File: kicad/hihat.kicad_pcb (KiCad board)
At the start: 2 copper layers, 174.5 x 173.5 mm, 172 parts, among them J1 Synth_power_2x5, J10 brain_south, J11 CVin, J2 CH trig, J3 accent, J4 CH out, J5 ctrl_north, J6 brain_north, J7 OH trig, J8 OH out, J9 ctrl_south, Q1 BC556, Q10 BC546, Q11 BC546, Q12 BC546, Q13 BC546, Q14 2N3904, Q15 BC546, Q16 BC546, Q2 BC546, Q3 BC546, Q4 BC556, Q5 BC556, Q6 BC556, Q7 BC546, Q8 BC546, Q9 BC546, SW1 mute, U1 TL074, U2 LM7805_TO220, U4 TL074, U5 LM13700, U6 Vactrol, U7 40106, U8 TL074

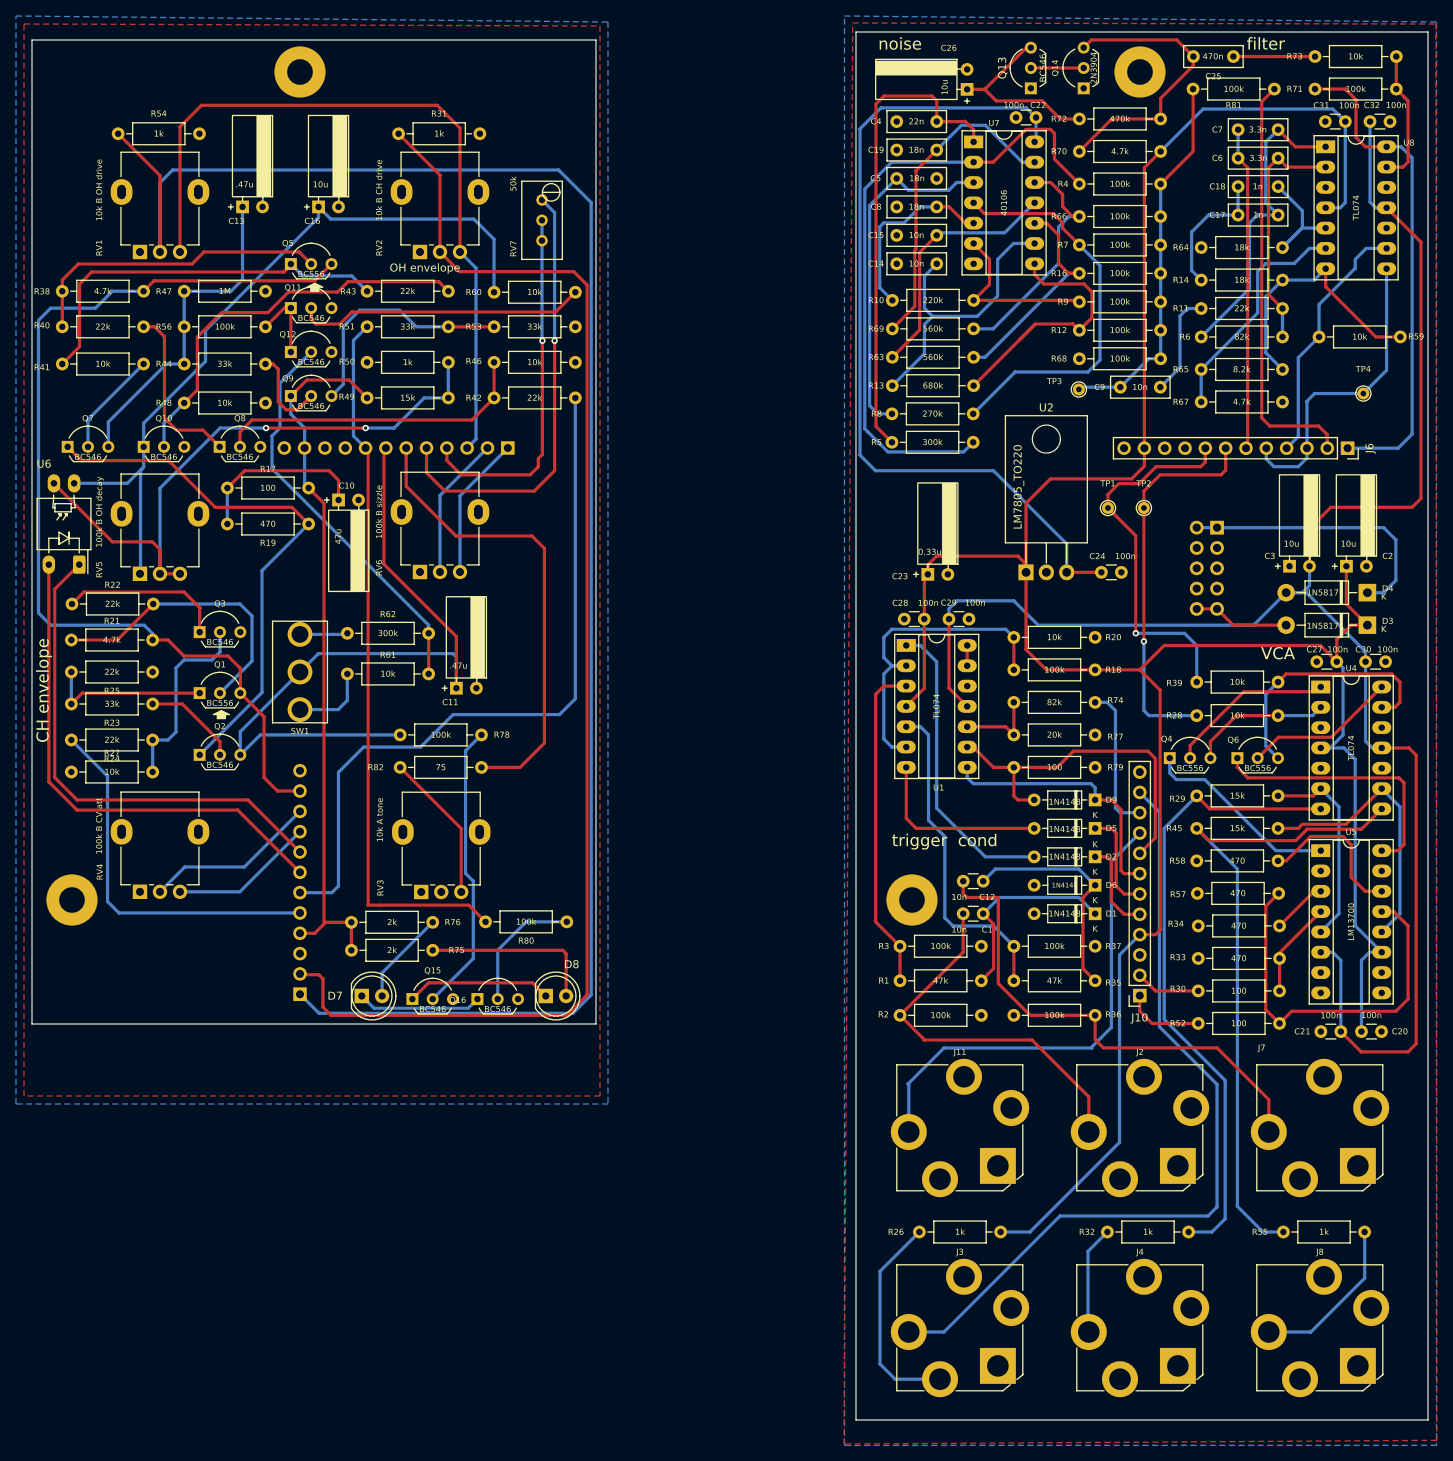
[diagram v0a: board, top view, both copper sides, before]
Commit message: fix noise section (1uF instead of 10uF), location of switch jacks!!, add resistor to make sizzle pot log-like and add note to use socket for cap to adjust tight decay
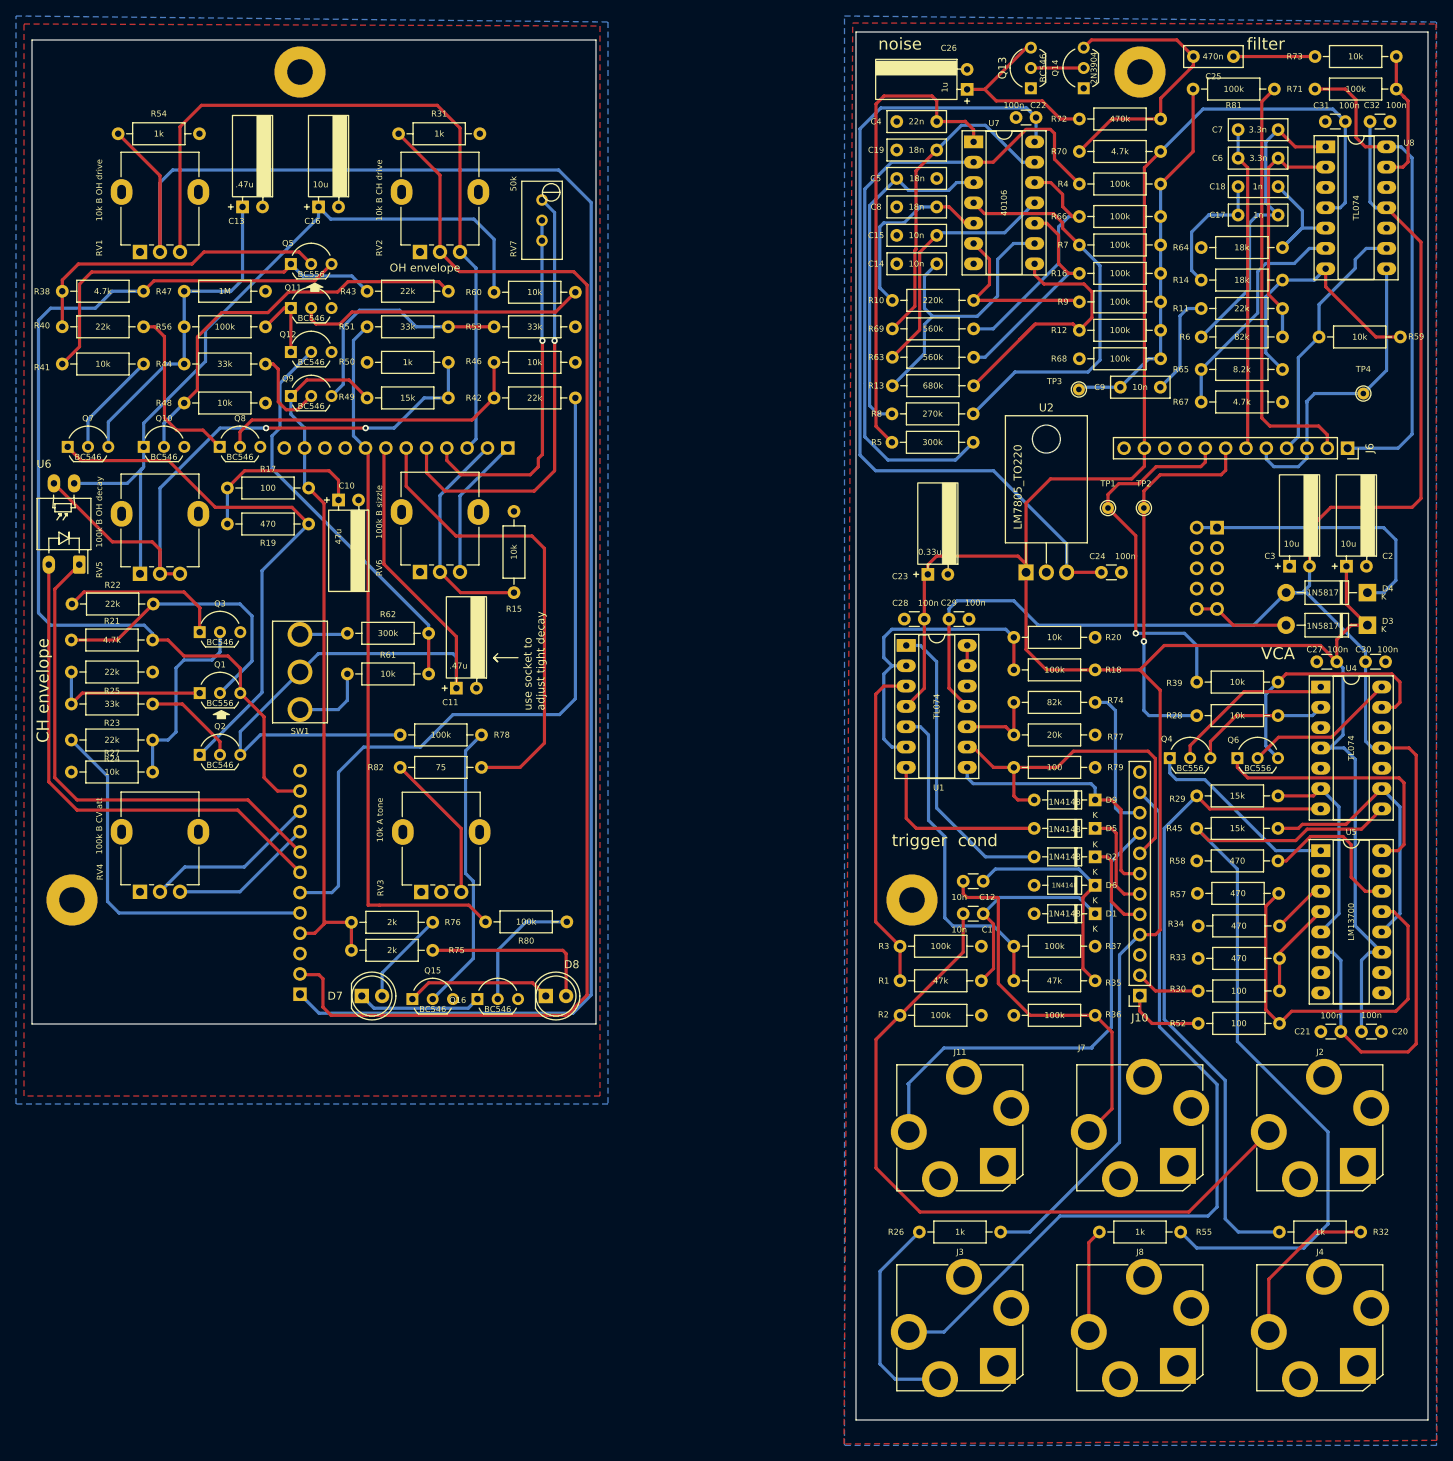
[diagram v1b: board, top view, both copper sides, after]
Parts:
- added R15: 10k, ao_tht:R_Axial_DIN0207_L6.3mm_D2.5mm_P10.16mm_Horizontal, F.Cu at (79.2, 100.6)
- C26: value 10u -> 1u
- moved R55 33.2 mm to (152.4, 180.5), turned to 0 degrees
- moved R32 31.7 mm to (185.1, 180.5), turned to 180 degrees
- moved J2 22.5 mm to (180.0, 167.5)
- moved J4 22.5 mm to (180.0, 192.5)
- moved J7 22.5 mm to (157.5, 167.5)
- moved J8 22.5 mm to (157.5, 192.5)
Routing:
- net Net-(C1-Pad2): track 48.2 -> 91.8 mm
- net Net-(R45-Pad1): track 81.8 -> 102.1 mm
- net Net-(C12-Pad2): track 62.5 -> 47.3 mm
- net white_noise_att_ctrl: track 18.0 -> 28.3 mm
- net Net-(J8-PadT): track 20.6 -> 13.0 mm
- net Net-(J4-PadT): track 13.5 -> 20.5 mm
- net Net-(R29-Pad1): track 79.1 -> 81.3 mm
- net Net-(R4-Pad1): track 79.7 -> 81.1 mm
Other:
- board text added: "use socket to adjust tight decay"

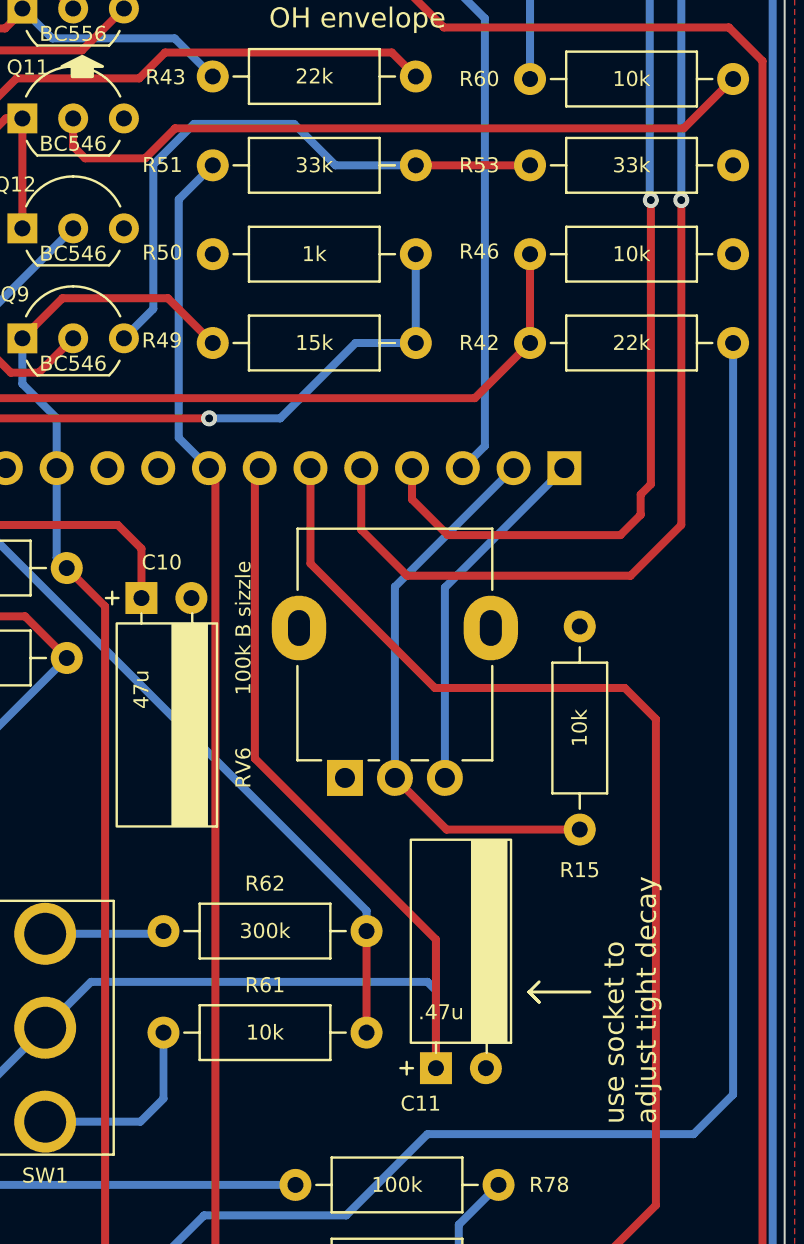
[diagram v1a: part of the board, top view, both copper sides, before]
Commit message: remove R51, now the open hat is much louder!
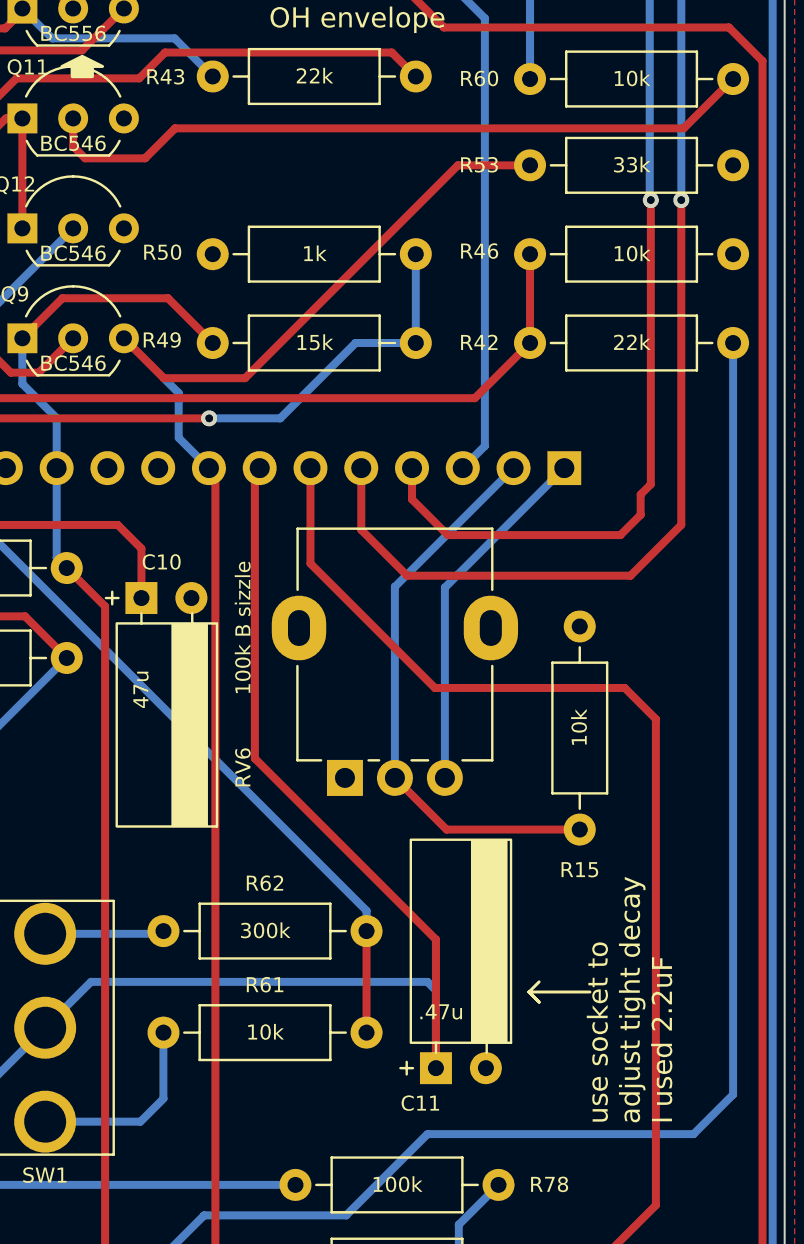
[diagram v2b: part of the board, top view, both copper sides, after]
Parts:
- removed R51: 33k, ao_tht:R_Axial_DIN0207_L6.3mm_D2.5mm_P10.16mm_Horizontal
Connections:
- Q9 pad 3: Net-(Q9-Pad3) -> OH_env_ctrl
- R53 pad 1: Net-(Q9-Pad3) -> OH_env_ctrl
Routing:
- net Net-(Q9-Pad3): track 29.9 -> 0.00 mm
- net OH_env_ctrl: track 89.3 -> 106.6 mm
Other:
- board text added: "use socket to adjust tight decay I used 2.2uF"
- board text removed: "use socket to adjust tight decay"

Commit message: change resistors in filter 18k to 20k
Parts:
- R14, R64: value 18k -> 20k
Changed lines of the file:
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@@
       (effects (font (size 0.75 0.75) (thickness 0.15)))
     )
-    (fp_text value "18k" (at 5.08 2.37) (layer "F.Fab")
+    (fp_text value "20k" (at 5.08 2.37) (layer "F.Fab")
       (effects (font (size 1 1) (thickness 0.15)))
     )
@@
       (effects (font (size 0.75 0.75) (thickness 0.15)))
     )
-    (fp_text value "18k" (at 5.08 2.37) (layer "F.Fab")
+    (fp_text value "20k" (at 5.08 2.37) (layer "F.Fab")
       (effects (font (size 1 1) (thickness 0.15)))
     )
